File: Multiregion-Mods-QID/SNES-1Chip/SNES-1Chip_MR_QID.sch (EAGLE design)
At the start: 42 parts, among them IC1 74HC27D, IC2 74HC30D

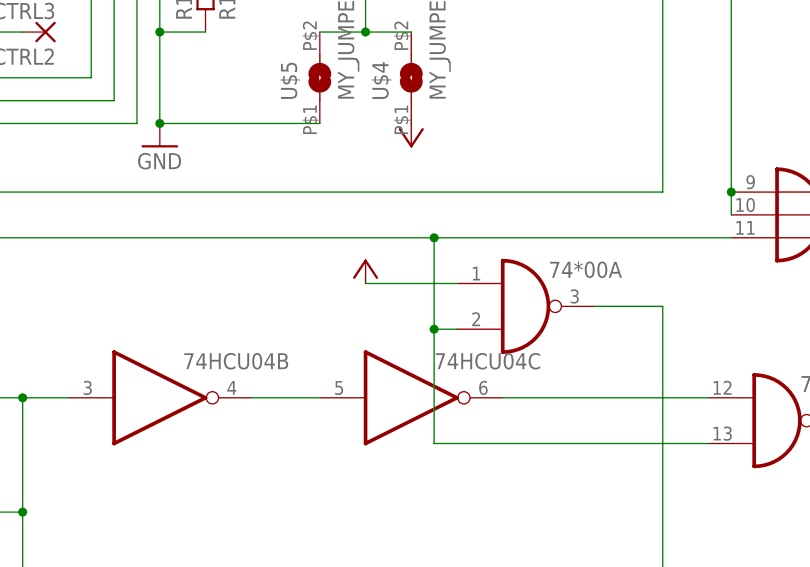
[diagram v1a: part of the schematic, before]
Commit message: add thermals to ground pad (easier to solder) and reduce PCB size a bit
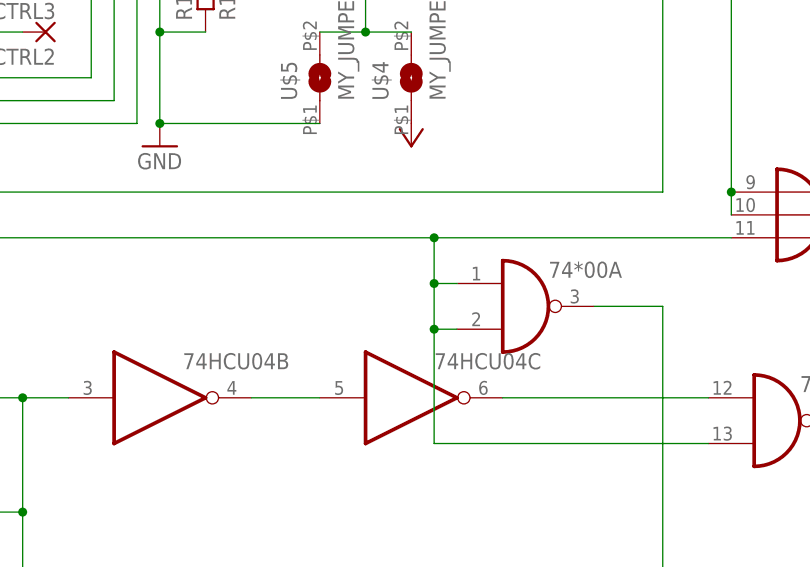
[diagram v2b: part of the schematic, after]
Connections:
- net N$14: now also 74*00A.I0
- net VCC: no longer 74*00A.I0
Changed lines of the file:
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@@
 <part name="GND2" library="supply1" deviceset="GND" device=""/>
 <part name="GND3" library="supply1" deviceset="GND" device=""/>
-<part name="VCC2" library="supply1" deviceset="+5V" device="" value=""/>
 <part name="R1" library="snescart" deviceset="R0805" device="" value="R10k"/>
 <part name="R2" library="snescart" deviceset="R0805" device="" value="R220"/>
@@
 <instance part="GND2" gate="1" x="124.46" y="-17.78"/>
 <instance part="GND3" gate="1" x="-78.74" y="-137.16"/>
-<instance part="VCC2" gate="1" x="7.62" y="-48.26"/>
 <instance part="R1" gate="G$1" x="-10.16" y="-17.78" rot="R90"/>
 <instance part="R2" gate="G$1" x="-81.28" y="-27.94" rot="R180"/>
@@
 <pinref part="U$4" gate="G$1" pin="1"/>
 </segment>
-<segment>
-<pinref part="VCC2" gate="1" pin="+5V"/>
-<pinref part="74*00" gate="A" pin="I0"/>
-<wire x1="7.62" y1="-50.8" x2="17.78" y2="-50.8" width="0.1524" layer="91"/>
-</segment>
 </net>
 <net name="N$2" class="0">
@@
 <segment>
 <wire x1="48.26" y1="-45.72" x2="15.24" y2="-45.72" width="0.1524" layer="91"/>
-<wire x1="15.24" y1="-45.72" x2="15.24" y2="-55.88" width="0.1524" layer="91"/>
+<wire x1="15.24" y1="-45.72" x2="15.24" y2="-50.8" width="0.1524" layer="91"/>
 <pinref part="74*00" gate="D" pin="I1"/>
+<wire x1="15.24" y1="-50.8" x2="15.24" y2="-55.88" width="0.1524" layer="91"/>
 <wire x1="15.24" y1="-55.88" x2="15.24" y2="-68.58" width="0.1524" layer="91"/>
 <wire x1="15.24" y1="-68.58" x2="45.72" y2="-68.58" width="0.1524" layer="91"/>
@@
 <junction x="-71.12" y="-20.32"/>
 <pinref part="IC1" gate="C" pin="I2"/>
-</segment>
-</net>
+<pinref part="74*00" gate="A" pin="I0"/>
+<wire x1="17.78" y1="-50.8" x2="15.24" y2="-50.8" width="0.1524" layer="91"/>
+<junction x="15.24" y="-50.8"/>
+</segment>
+</net>
